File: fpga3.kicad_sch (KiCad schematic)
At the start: 3 parts, among them P1 5CEFA7F23

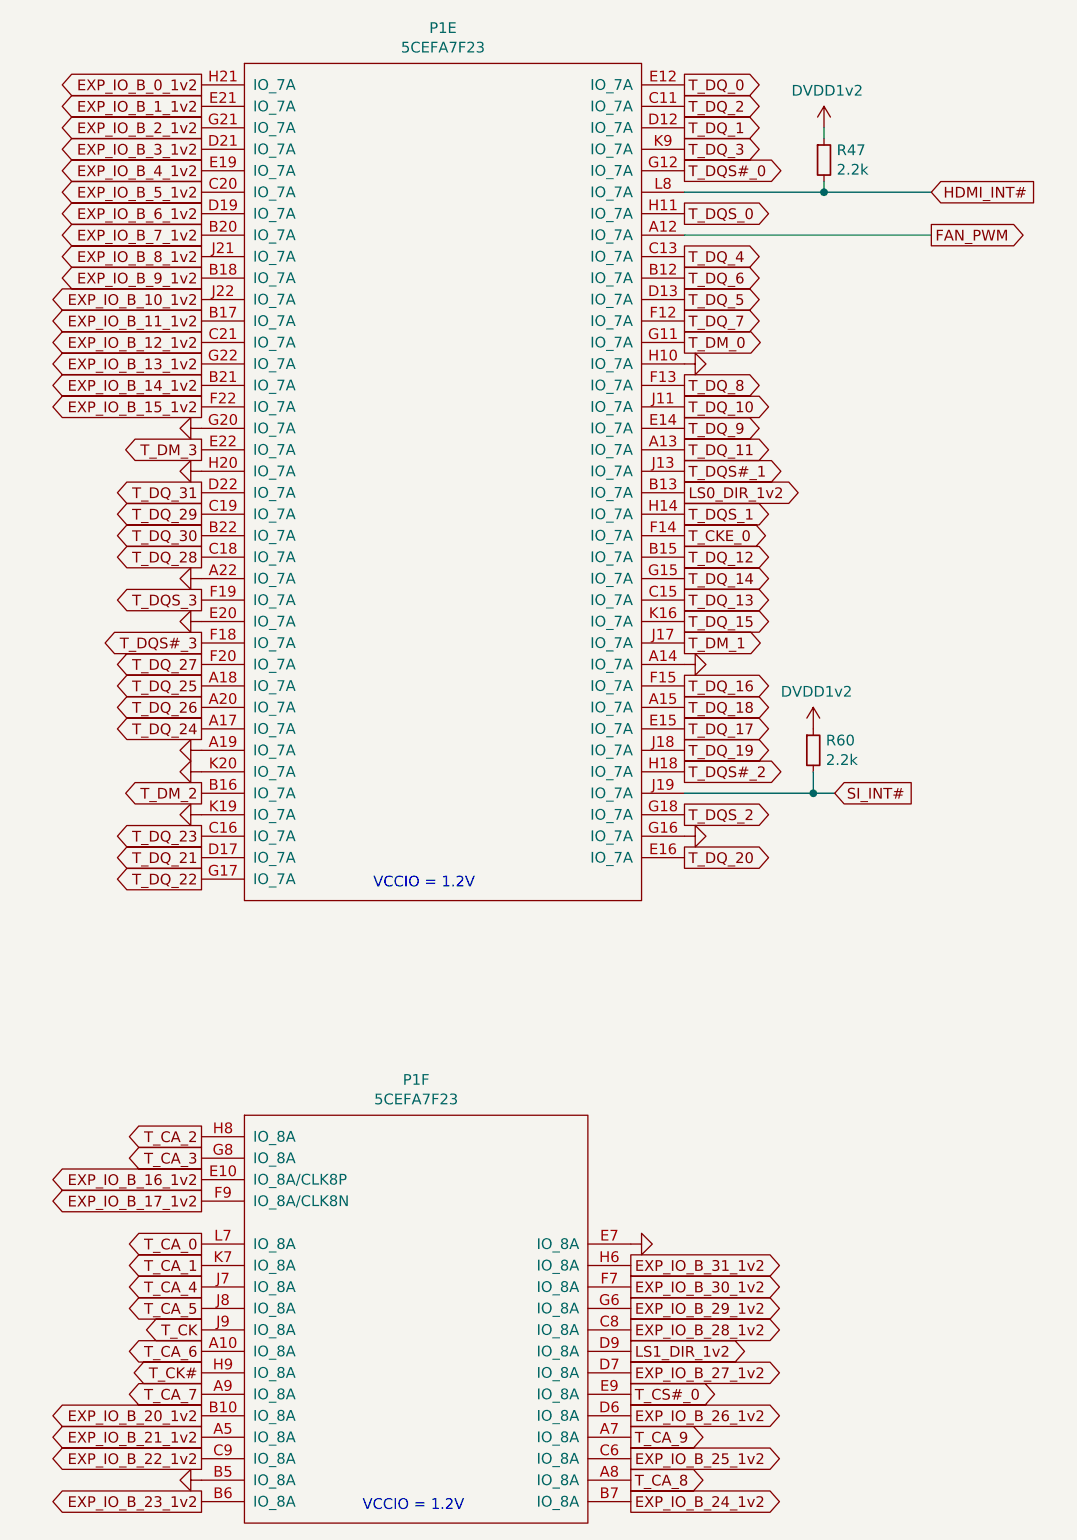
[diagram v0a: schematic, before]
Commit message: update schematic to v1.5
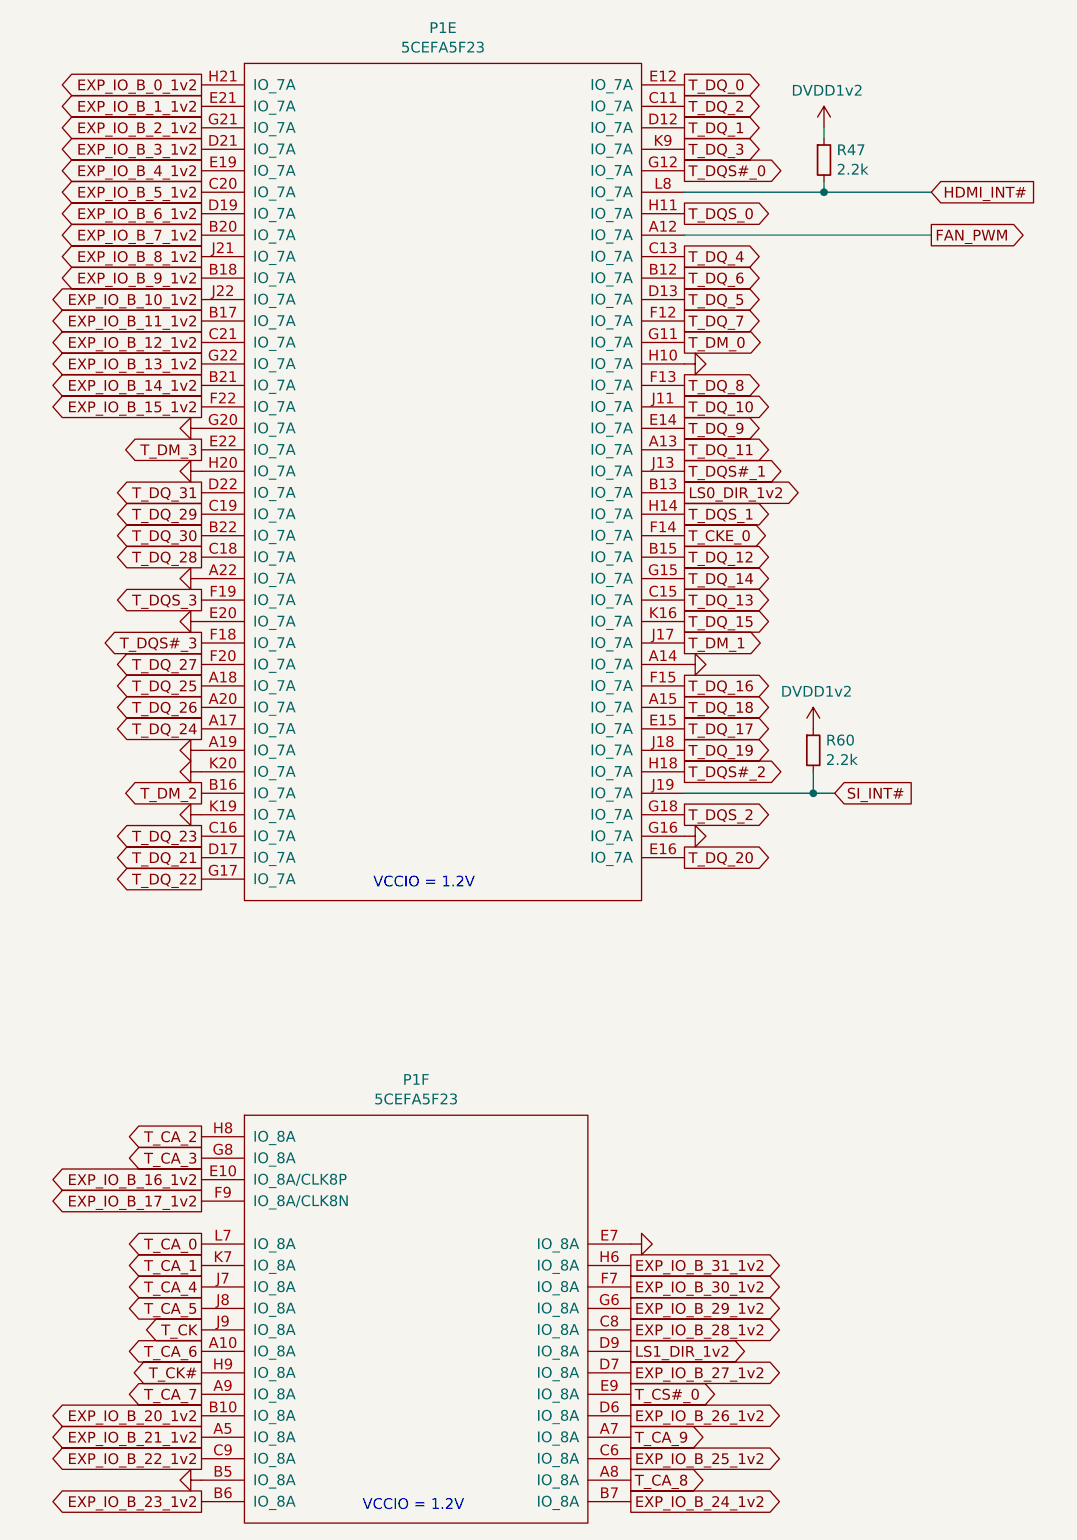
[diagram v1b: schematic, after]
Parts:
- P1: value 5CEFA7F23 -> 5CEFA5F23
